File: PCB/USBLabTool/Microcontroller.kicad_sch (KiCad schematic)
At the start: 2 parts, among them P1 USB_C_Plug_USB2.0, U11 STM32H563RGTx

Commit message: Starting PCB layout
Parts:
- removed P1: USB_C_Plug_USB2.0, symbol Connector:USB_C_Plug_USB2.0
- removed U11: STM32H563RGTx, Package_QFP:LQFP-64_10x10mm_P0.5mm, symbol MCU_ST_STM32H5:STM32H563RGTx
- added R54, R55: 22, Resistor_SMD:R_0603_1608Metric_Pad0.98x0.95mm_HandSolder, symbol Device:R
- added U13: STM32H562RGTx, Package_QFP:LQFP-64_10x10mm_P0.5mm, symbol MCU_ST_STM32H5:STM32H562RGTx
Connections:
- new net: U13.18 (VSS), U13.31 (VSS), U13.47 (VSS), U13.63 (VSS)
- new net: R54.1, U13.44 (PA11)
- new net: R55.1, U13.45 (PA12)
- new net +3.3V: U13.1 (VBAT), U13.19 (VDD), U13.32 (VDD), U13.48 (VDD), U13.64 (VDD)
- new net ADC1: U13.14 (PA0)
- new net ADC2: U13.23 (PA7)
- new net CH0 ACDC: U13.34 (PB13)
- new net CH0_attenuate: U13.35 (PB14)
- new net CH1 ACDC: U13.24 (PC4)
- new net CH1_attenuate: U13.25 (PC5)
- new net DAC1: U13.20 (PA4)
- new net DAC2: U13.21 (PA5)
- new net GAIN_C0: U13.17 (PA3)
- new net GAIN_C1: U13.22 (PA6)
- new net GND: U13.12 (VSSA)
- new net RCC_OSC32_IN: U13.3 (PC14)
- new net RCC_OSC32_OUT: U13.4 (PC15)
- new net RCC_OSC_IN: U13.5 (PH0)
- new net RCC_OSC_OUT: U13.6 (PH1)
- new net TIM1_CH1: U13.41 (PA8)
- new net TIM1_CH2: U13.42 (PA9)
- new net TIM2_CH1: U13.50 (PA15(JTDI))
- new net TIM2_CH2: U13.15 (PA1)
- new net USB_DM: R54.2
- new net USB_DP: R55.2
- new net amp1-1: U13.36 (PB15)
- new net amp1-10: U13.33 (PB12)
- new net amp1-2.5: U13.37 (PC6)
- new net amp1-5: U13.39 (PC8)
- new net amp2-1: U13.29 (PB10)
- new net amp2-10: U13.26 (PB0)
- new net amp2-2.5: U13.28 (PB2)
- new net amp2-5: U13.27 (PB1)
- no-connect marks 0 -> 27
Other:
- note added: "recheck the USB footprint later, placeholder at the moment."

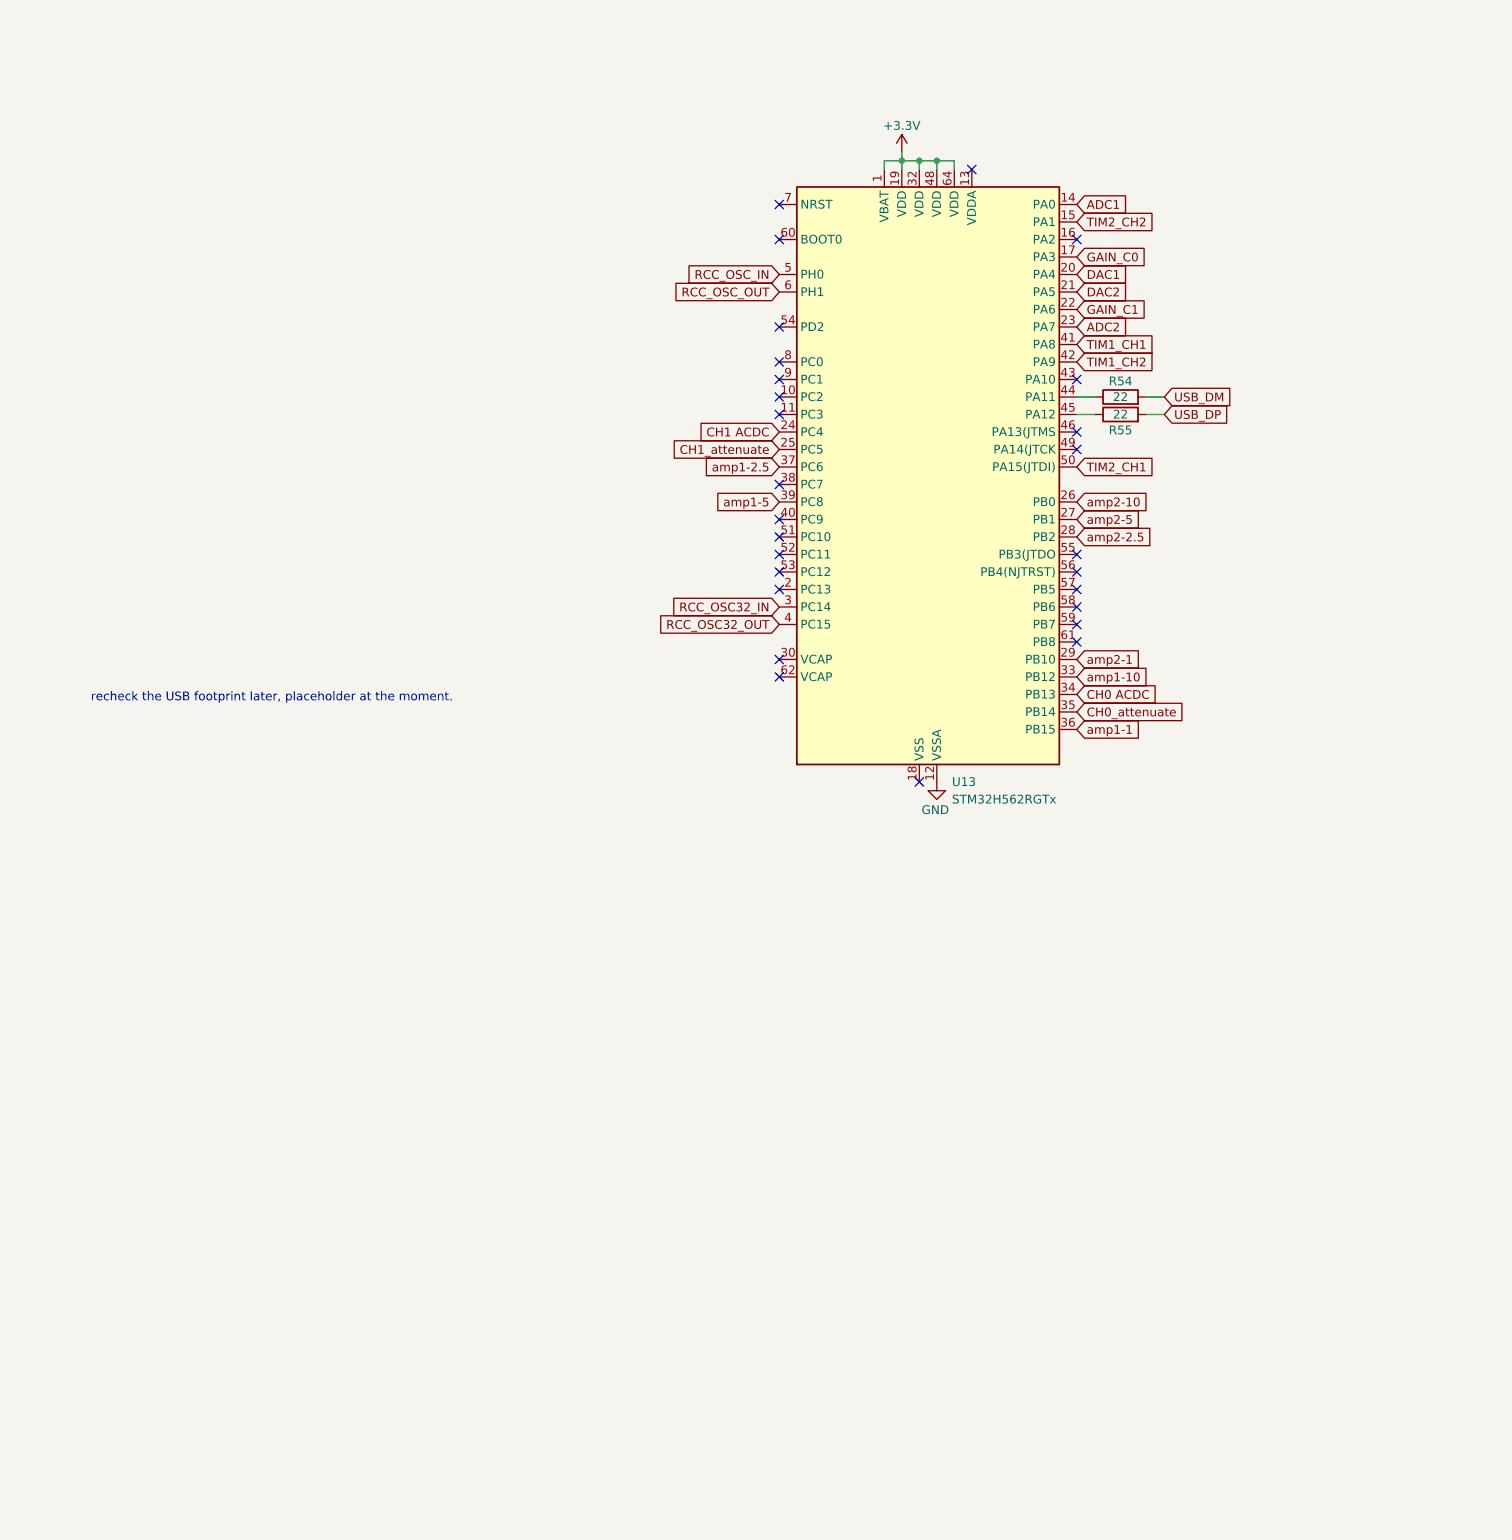
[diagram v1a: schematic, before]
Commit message: Moving files to where they should be
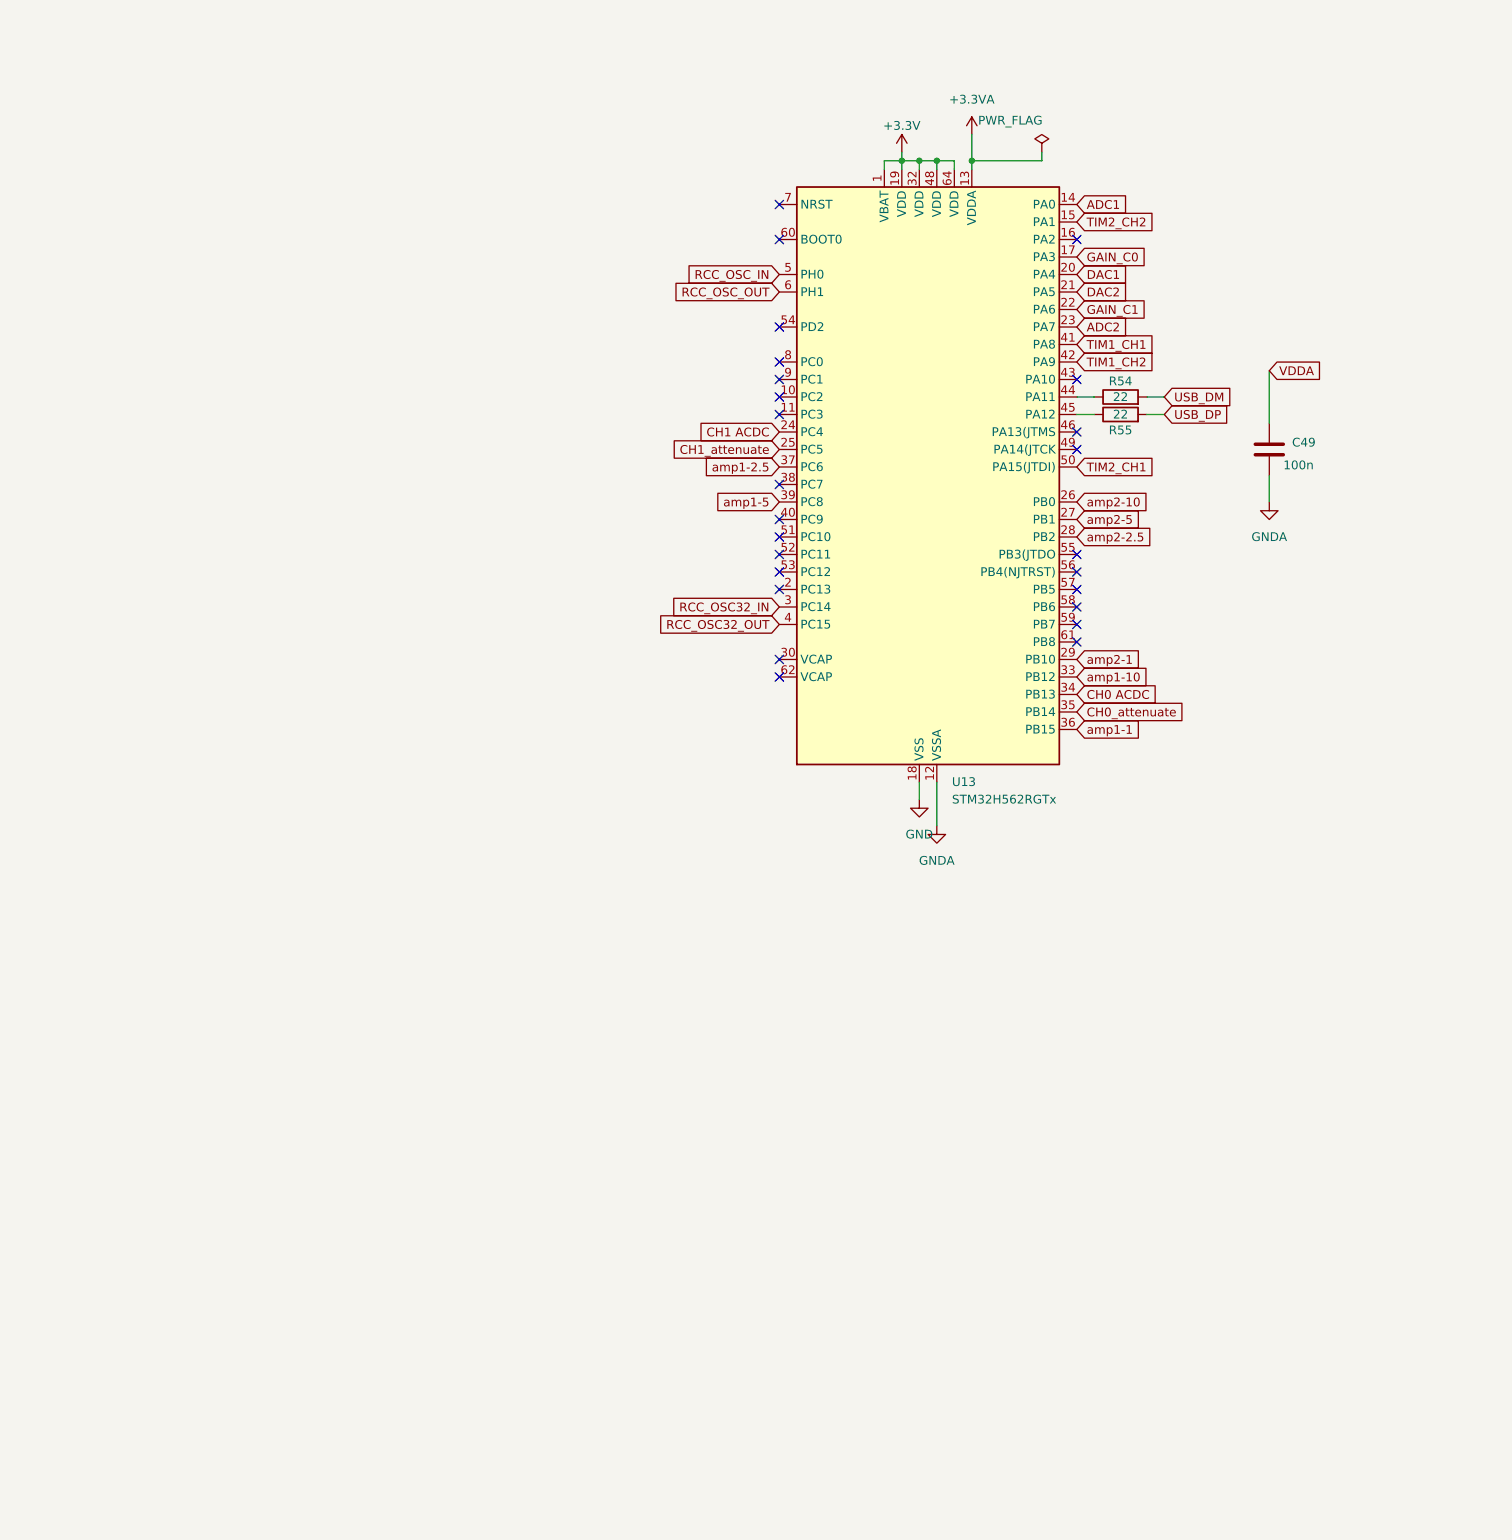
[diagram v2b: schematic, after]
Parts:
- added C49: 100n, Capacitor_SMD:C_0603_1608Metric_Pad1.08x0.95mm_HandSolder, symbol Device:C
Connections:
- net GND: now also U13.18 (VSS), U13.31 (VSS), U13.47 (VSS), U13.63 (VSS); no longer U13.12 (VSSA)
- net +3.3VA: now reaches U13.13 (VDDA)
- new net GNDA: C49.2, U13.12 (VSSA)
- new net VDDA: C49.1
- no-connect marks 27 -> 25
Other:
- note removed: "recheck the USB footprint later, placeholder at the moment."

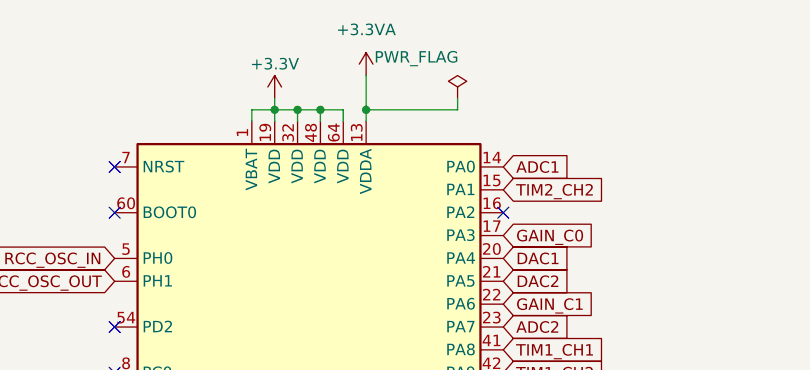
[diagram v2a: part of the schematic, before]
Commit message: Moving files to where they should be
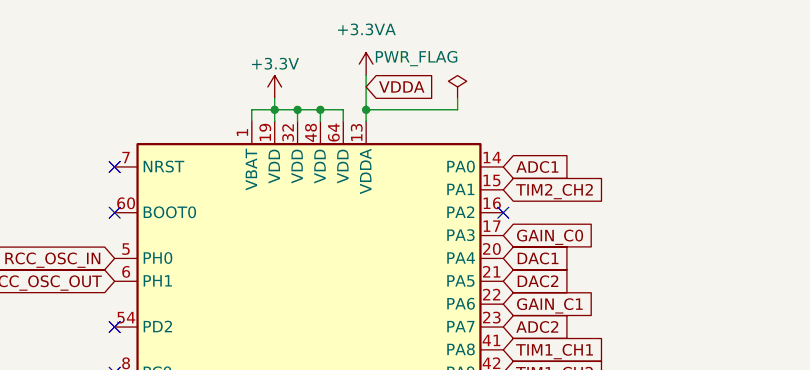
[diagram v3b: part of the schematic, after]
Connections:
- net VDDA is gone; now on net +3.3VA: C49.1
